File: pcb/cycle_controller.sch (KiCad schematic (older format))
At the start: 38 parts

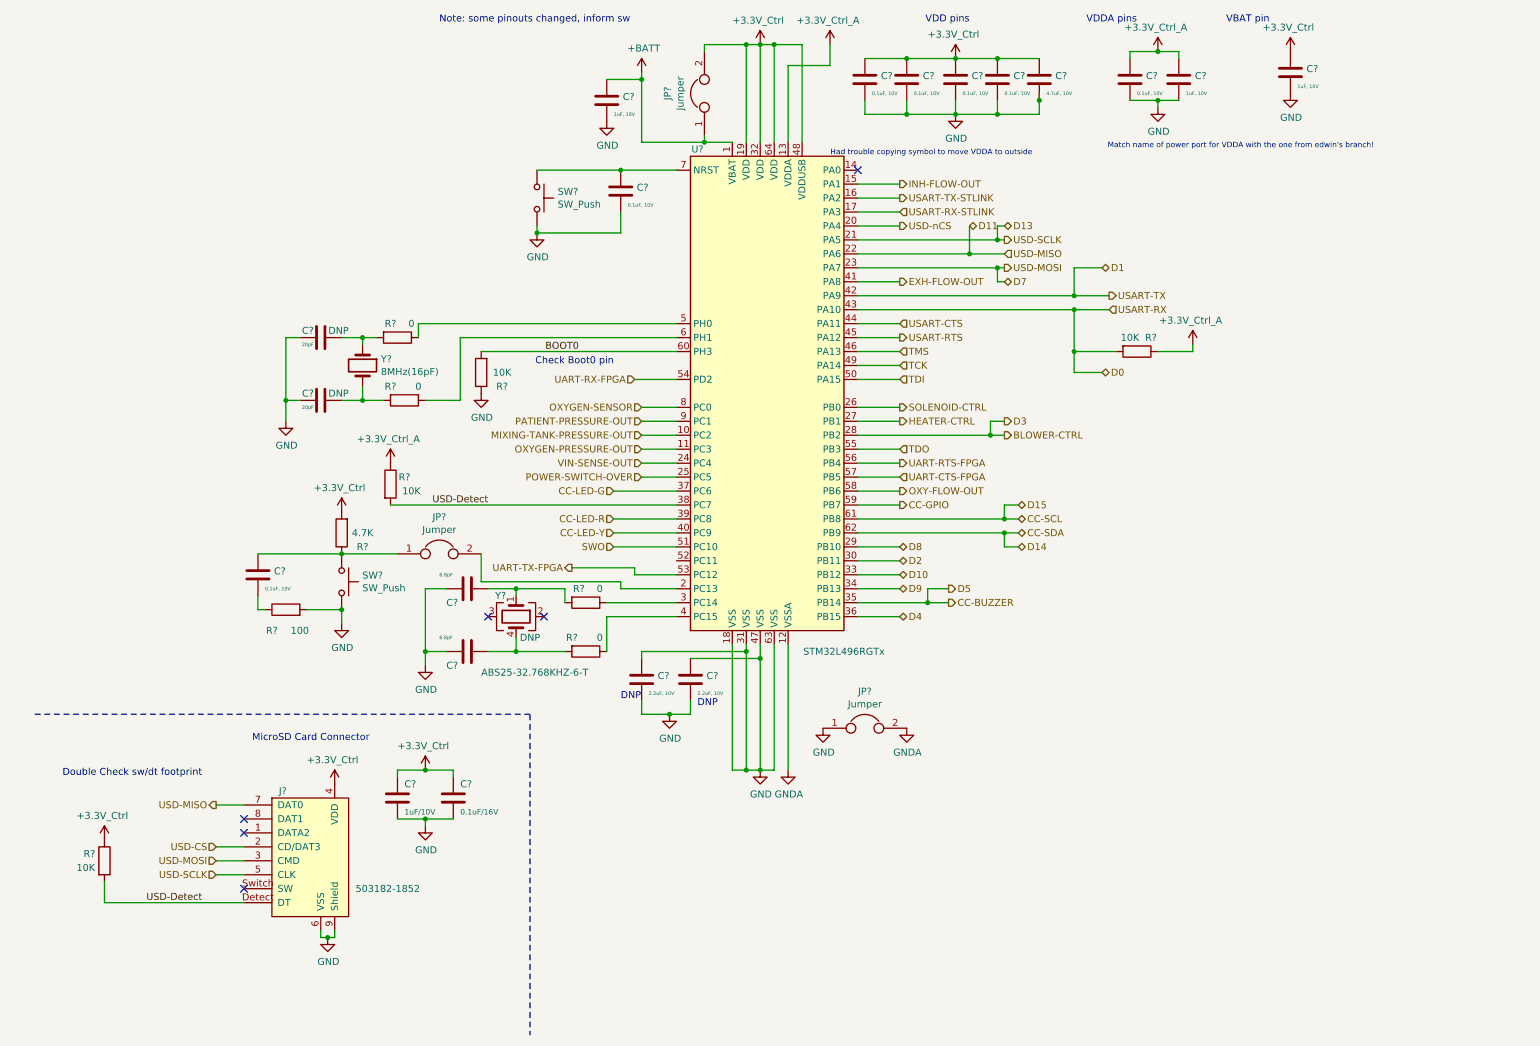
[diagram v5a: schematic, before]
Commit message: cycle controller updates, added headers to page
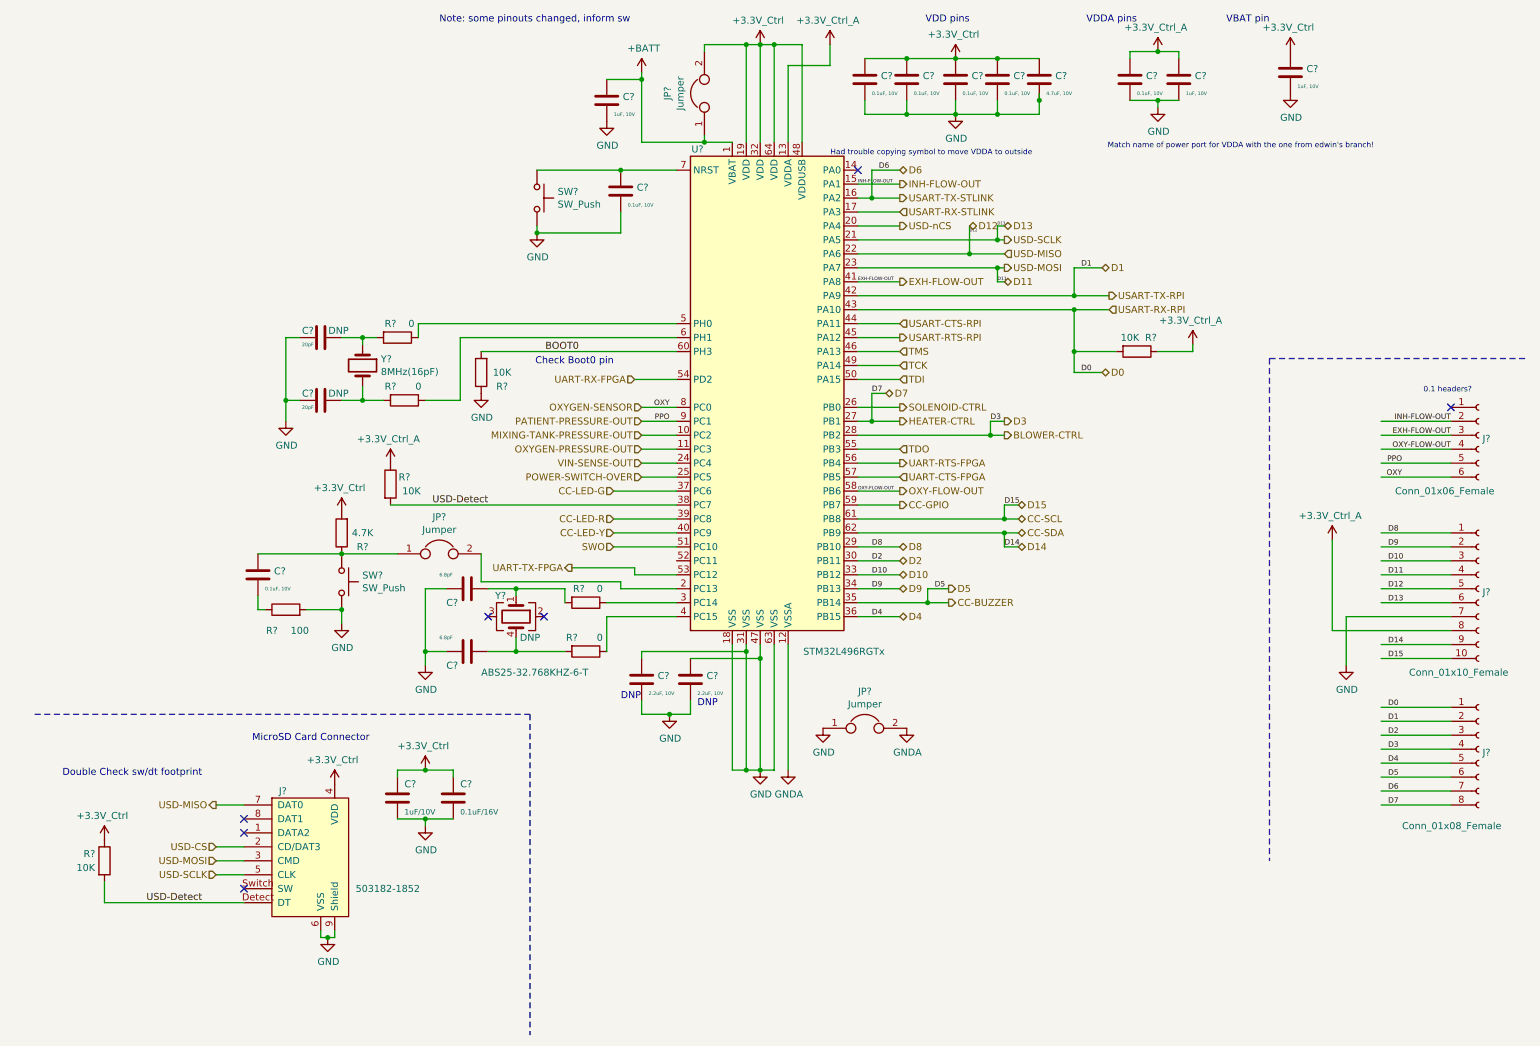
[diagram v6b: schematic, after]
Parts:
- added J?: Conn_01x10_Female, symbol Connector:Conn_01x10_Female
- added J?: Conn_01x08_Female, symbol Connector:Conn_01x08_Female
- added J?: Conn_01x06_Female, symbol Connector:Conn_01x06_Female
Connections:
- net labels added: D12, D6, OXY, PPO, USART-CTS-RPI, USART-RTS-RPI, USART-RX-RPI, USART-TX-RPI
- net labels removed: USART-CTS, USART-RTS, USART-RX, USART-TX
- wire segments 194 -> 225
- no-connect marks 6 -> 7
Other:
- note added: "0.1 headers?"
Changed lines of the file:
@@
 NoConn ~ 3750 4800
 Text HLabel 8200 2500 2    50   Output ~ 0
-USART-TX
+USART-TX-RPI
 Text HLabel 8200 2600 2    50   Input ~ 0
-USART-RX
+USART-RX-RPI
 Text HLabel 6700 2700 2    50   Input ~ 0
-USART-CTS
+USART-CTS-RPI
 Text HLabel 6700 2800 2    50   Output ~ 0
-USART-RTS
+USART-RTS-RPI
 Wire Wire Line
 	8200 2600 7950 2600
@@
 USART-RX-STLINK
 Wire Wire Line
-	6400 1800 6700 1800
+	6400 1800 6500 1800
 Wire Wire Line
 	6400 1900 6700 1900
@@
 	6400 3300 6700 3300
 Wire Wire Line
-	6400 3400 6700 3400
+	6400 3400 6500 3400
 Text HLabel 7450 3500 2    50   Output ~ 0
 BLOWER-CTRL
@@
 	7450 3400 7350 3400
 Text HLabel 7450 2400 2    50   BiDi ~ 0
-D7
+D11
 Wire Wire Line
 	7400 2300 7450 2300
@@
 	7400 2400 7450 2400
 Text HLabel 7200 2000 2    50   BiDi ~ 0
-D11
+D12
 Wire Wire Line
 	7200 2200 7450 2200
@@
 Wire Wire Line
 	7950 2900 7950 3050
+$Comp
+L Connector:Conn_01x10_Female J?
+U 1 1 602AB666
+P 10850 4600
+F 0 "J?" H 10877 4576 50  0000 L CNN
+F 1 "Conn_01x10_Female" H 10350 4000 50  0000 L CNN
+F 2 "" H 10850 4600 50  0001 C CNN
+F 3 "~" H 10850 4600 50  0001 C CNN
+	1    10850 4600
+	1    0    0    -1
+$EndComp
+$Comp
+L Connector:Conn_01x08_Female J?
+U 1 1 602AB6F0
+P 10850 5750
+F 0 "J?" H 10877 5726 50  0000 L CNN
+F 1 "Conn_01x08_Female" H 10300 5200 50  0000 L CNN
+F 2 "" H 10850 5750 50  0001 C CNN
+F 3 "~" H 10850 5750 50  0001 C CNN
+	1    10850 5750
+	1    0    0    -1
+$EndComp
+$Comp
+L Connector:Conn_01x06_Female J?
+U 1 1 602AB793
+P 10850 3500
+F 0 "J?" H 10877 3476 50  0000 L CNN
+F 1 "Conn_01x06_Female" H 10250 3100 50  0000 L CNN
+F 2 "" H 10850 3500 50  0001 C CNN
+F 3 "~" H 10850 3500 50  0001 C CNN
+	1    10850 3500
+	1    0    0    -1
+$EndComp
+Text Notes 10800 3200 2    39   ~ 0
+0.1 headers?
+Wire Notes Line
+	9350 2950 9350 6550
+NoConn ~ 10650 3300
+Wire Wire Line
+	10650 3400 10150 3400
+Wire Wire Line
+	10650 3500 10150 3500
+Wire Wire Line
+	10650 3600 10150 3600
+Wire Wire Line
+	10650 3700 10150 3700
+Wire Wire Line
+	10650 3800 10150 3800
+Text Label 10650 3400 2    39   ~ 0
+INH-FLOW-OUT
+Text Label 6400 1700 0    24   ~ 0
+INH-FLOW-OUT
+Text Label 6400 2400 0    24   ~ 0
+EXH-FLOW-OUT
+Text Label 10650 3500 2    39   ~ 0
+EXH-FLOW-OUT
+Text Label 6400 3900 0    24   ~ 0
+OXY-FLOW-OUT
+Text Label 10650 3600 2    39   ~ 0
+OXY-FLOW-OUT
+Text Label 5050 3400 2    39   ~ 0
+PPO
+Text Label 10300 3700 2    39   ~ 0
+PPO
+Text Label 5050 3300 2    39   ~ 0
+OXY
+Text Label 10300 3800 2    39   ~ 0
+OXY
+Text HLabel 6600 3200 2    50   BiDi ~ 0
+D7
+Wire Wire Line
+	6600 3200 6500 3200
+Wire Wire Line
+	6500 3200 6500 3400
+Connection ~ 6500 3400
+Wire Wire Line
+	6500 3400 6700 3400
+Wire Wire Line
+	10650 4200 10150 4200
+Wire Wire Line
+	10650 4300 10150 4300
+Wire Wire Line
+	10650 4400 10150 4400
+Wire Wire Line
+	10650 4500 10150 4500
+Wire Wire Line
+	10650 4600 10150 4600
+Wire Wire Line
+	10650 4700 10150 4700
+Wire Wire Line
+	10650 5000 10150 5000
+Wire Wire Line
+	10650 5100 10150 5100
+Text Label 10200 4200 0    39   ~ 0
+D8
+Text Label 10200 4300 0    39   ~ 0
+D9
+Text Label 10200 4400 0    39   ~ 0
+D10
+Text Label 10200 4500 0    39   ~ 0
+D11
+Text Label 10200 4600 0    39   ~ 0
+D12
+Text Label 10200 4700 0    39   ~ 0
+D13
+Text Label 10200 5000 0    39   ~ 0
+D14
+Text Label 10200 5100 0    39   ~ 0
+D15
+$Comp
+L RespiraWorks:+3.3V_Ctrl_A #PWR?
+U 1 1 60390EE2
+P 9800 4250
+F 0 "#PWR?" H 9800 4250 50  0001 C CNN
+F 1 "+3.3V_Ctrl_A" H 9785 4423 50  0000 C CNN
+F 2 "" H 9800 4250 50  0001 C CNN
+F 3 "" H 9800 4250 50  0001 C CNN
+	1    9800 4250
+	1    0    0    -1
+$EndComp
+$Comp
+L power:GND #PWR?
+U 1 1 60390FBB
+P 9900 5150
+F 0 "#PWR?" H 9900 4900 50  0001 C CNN
+F 1 "GND" H 9905 4977 50  0000 C CNN
+F 2 "" H 9900 5150 50  0001 C CNN
+F 3 "" H 9900 5150 50  0001 C CNN
+	1    9900 5150
+	1    0    0    -1
+$EndComp
+Wire Wire Line
+	10650 4800 9900 4800
+Wire Wire Line
+	9900 4800 9900 5150
+Wire Wire Line
+	10650 4900 9800 4900
+Wire Wire Line
+	9800 4900 9800 4250
+Wire Notes Line
+	9350 2950 11200 2950
+Text Label 6500 4300 0    39   ~ 0
+D8
+Text Label 6500 4600 0    39   ~ 0
+D9
+Text Label 6500 4500 0    39   ~ 0
+D10
+Text Label 6500 4400 0    39   ~ 0
+D2
+Text Label 6500 4800 0    39   ~ 0
+D4
+Text Label 7450 4300 0    39   ~ 0
+D14
+Text Label 7450 4000 0    39   ~ 0
+D15
+Text Label 7350 3400 0    39   ~ 0
+D3
+Text Label 6500 3200 0    39   ~ 0
+D7
+Text Label 8000 3050 0    39   ~ 0
+D0
+Text Label 8000 2300 0    39   ~ 0
+D1
+Text Label 7400 2400 0    24   ~ 0
+D11
+Text Label 7400 2000 0    20   ~ 0
+D13
+Text Label 7200 2050 0    20   ~ 0
+D12
+Wire Wire Line
+	10650 5450 10150 5450
+Wire Wire Line
+	10650 5550 10150 5550
+Wire Wire Line
+	10650 5650 10150 5650
+Wire Wire Line
+	10650 5750 10150 5750
+Wire Wire Line
+	10650 5850 10150 5850
+Wire Wire Line
+	10650 5950 10150 5950
+Wire Wire Line
+	10650 6050 10150 6050
+Wire Wire Line
+	10650 6150 10150 6150
+Text Label 10200 5450 0    39   ~ 0
+D0
+Text Label 10200 5550 0    39   ~ 0
+D1
+Text Label 10200 5650 0    39   ~ 0
+D2
+Text Label 10200 5750 0    39   ~ 0
+D3
+Text Label 10200 5850 0    39   ~ 0
+D4
+Text Label 10200 6150 0    39   ~ 0
+D7
+Text Label 6950 4600 0    39   ~ 0
+D5
+Text Label 10200 5950 0    39   ~ 0
+D5
+Text HLabel 6700 1600 2    50   BiDi ~ 0
+D6
+Wire Wire Line
+	6700 1600 6500 1600
+Wire Wire Line
+	6500 1600 6500 1800
+Connection ~ 6500 1800
+Wire Wire Line
+	6500 1800 6700 1800
+Text Label 6550 1600 0    39   ~ 0
+D6
+Text Label 10200 6050 0    39   ~ 0
+D6
 $EndSCHEMATC

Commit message: ui computer
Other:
- moved on the sheet: C?, J?, R?
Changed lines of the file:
@@
 L RespiraWorks:503182-1852 J?
 U 1 1 6016937E
-P 2450 6400
+P 2500 6650
 AR Path="/5FCD4D4C/6016937E" Ref="J?"  Part="1"
 AR Path="/5FCD4D18/6016937E" Ref="J?"  Part="1"
-F 0 "J?" H 2250 6750 50  0000 L CNN
-F 1 "503182-1852" H 2800 6050 50  0000 L CNN
-F 2 "RespiraWorks:5031821852" H 3250 6000 50  0001 C CNN
-F 3 "https://www.molex.com/pdm_docs/sd/5031821852_sd.pdf" H 3850 5900 50  0001 C CNN
-	1    2450 6400
+F 0 "J?" H 2300 7000 50  0000 L CNN
+F 1 "503182-1852" H 2850 6300 50  0000 L CNN
+F 2 "RespiraWorks:5031821852" H 3300 6250 50  0001 C CNN
+F 3 "https://www.molex.com/pdm_docs/sd/5031821852_sd.pdf" H 3900 6150 50  0001 C CNN
+	1    2500 6650
 	1    0    0    -1
 $EndComp
-Text Notes 2900 5700 2    50   ~ 0
+Text Notes 2950 5950 2    50   ~ 0
 MicroSD Card Connector
 $Comp
 L RespiraWorks:+3.3V_Ctrl #PWR?
 U 1 1 60169386
-P 2650 6000
+P 2700 6250
 AR Path="/5FCD4D4C/60169386" Ref="#PWR?"  Part="1"
 AR Path="/5FCD4D18/60169386" Ref="#PWR?"  Part="1"
-F 0 "#PWR?" H 2650 6000 50  0001 C CNN
-F 1 "+3.3V_Ctrl" H 2635 6173 50  0000 C CNN
-F 2 "" H 2650 6000 50  0001 C CNN
-F 3 "" H 2650 6000 50  0001 C CNN
-	1    2650 6000
+F 0 "#PWR?" H 2700 6250 50  0001 C CNN
+F 1 "+3.3V_Ctrl" H 2685 6423 50  0000 C CNN
+F 2 "" H 2700 6250 50  0001 C CNN
+F 3 "" H 2700 6250 50  0001 C CNN
+	1    2700 6250
 	1    0    0    -1
 $EndComp
@@
 L Device:C C?
 U 1 1 6016938C
-P 3100 6100
+P 3150 6350
 AR Path="/5FCD4D4C/6016938C" Ref="C?"  Part="1"
 AR Path="/5FCD4D18/6016938C" Ref="C?"  Part="1"
-F 0 "C?" H 3150 6200 50  0000 L CNN
-F 1 "1uF/10V" H 3150 6000 39  0000 L CNN
-F 2 "" H 3138 5950 50  0001 C CNN
-F 3 "~" H 3100 6100 50  0001 C CNN
-	1    3100 6100
+F 0 "C?" H 3200 6450 50  0000 L CNN
+F 1 "1uF/10V" H 3200 6250 39  0000 L CNN
+F 2 "" H 3188 6200 50  0001 C CNN
+F 3 "~" H 3150 6350 50  0001 C CNN
+	1    3150 6350
 	1    0    0    -1
 $EndComp
@@
 L Device:C C?
 U 1 1 60169393
-P 3500 6100
+P 3550 6350
 AR Path="/5FCD4D4C/60169393" Ref="C?"  Part="1"
 AR Path="/5FCD4D18/60169393" Ref="C?"  Part="1"
-F 0 "C?" H 3550 6200 50  0000 L CNN
-F 1 "0.1uF/16V" H 3550 6000 39  0000 L CNN
-F 2 "" H 3538 5950 50  0001 C CNN
-F 3 "~" H 3500 6100 50  0001 C CNN
-	1    3500 6100
+F 0 "C?" H 3600 6450 50  0000 L CNN
+F 1 "0.1uF/16V" H 3600 6250 39  0000 L CNN
+F 2 "" H 3588 6200 50  0001 C CNN
+F 3 "~" H 3550 6350 50  0001 C CNN
+	1    3550 6350
 	1    0    0    -1
 $EndComp
@@
 L RespiraWorks:+3.3V_Ctrl #PWR?
 U 1 1 6016939A
-P 3300 5900
+P 3350 6150
 AR Path="/5FCD4D4C/6016939A" Ref="#PWR?"  Part="1"
 AR Path="/5FCD4D18/6016939A" Ref="#PWR?"  Part="1"
-F 0 "#PWR?" H 3300 5900 50  0001 C CNN
-F 1 "+3.3V_Ctrl" H 3285 6073 50  0000 C CNN
-F 2 "" H 3300 5900 50  0001 C CNN
-F 3 "" H 3300 5900 50  0001 C CNN
-	1    3300 5900
+F 0 "#PWR?" H 3350 6150 50  0001 C CNN
+F 1 "+3.3V_Ctrl" H 3335 6323 50  0000 C CNN
+F 2 "" H 3350 6150 50  0001 C CNN
+F 3 "" H 3350 6150 50  0001 C CNN
+	1    3350 6150
 	1    0    0    -1
 $EndComp
 Wire Wire Line
-	3100 5950 3100 5900
+	3150 6200 3150 6150
 Wire Wire Line
-	3100 5900 3300 5900
+	3150 6150 3350 6150
 Wire Wire Line
-	3300 5900 3500 5900
+	3350 6150 3550 6150
 Wire Wire Line
-	3500 5900 3500 5950
-Connection ~ 3300 5900
+	3550 6150 3550 6200
+Connection ~ 3350 6150
 $Comp
 L power:GND #PWR?
 U 1 1 601693A5
-P 3300 6300
+P 3350 6550
 AR Path="/5FCD4D4C/601693A5" Ref="#PWR?"  Part="1"
 AR Path="/5FCD4D18/601693A5" Ref="#PWR?"  Part="1"
-F 0 "#PWR?" H 3300 6050 50  0001 C CNN
-F 1 "GND" H 3305 6127 50  0000 C CNN
-F 2 "" H 3300 6300 50  0001 C CNN
-F 3 "" H 3300 6300 50  0001 C CNN
-	1    3300 6300
+F 0 "#PWR?" H 3350 6300 50  0001 C CNN
+F 1 "GND" H 3355 6377 50  0000 C CNN
+F 2 "" H 3350 6550 50  0001 C CNN
+F 3 "" H 3350 6550 50  0001 C CNN
+	1    3350 6550
 	1    0    0    -1
 $EndComp
 Wire Wire Line
-	3100 6250 3300 6250
+	3150 6500 3350 6500
 Wire Wire Line
-	3300 6250 3300 6300
+	3350 6500 3350 6550
 Wire Wire Line
-	3500 6250 3300 6250
-Connection ~ 3300 6250
+	3550 6500 3350 6500
+Connection ~ 3350 6500
 $Comp
 L power:GND #PWR?
 U 1 1 601693AF
-P 2600 7100
+P 2650 7350
 AR Path="/5FCD4D4C/601693AF" Ref="#PWR?"  Part="1"
 AR Path="/5FCD4D18/601693AF" Ref="#PWR?"  Part="1"
-F 0 "#PWR?" H 2600 6850 50  0001 C CNN
-F 1 "GND" H 2605 6927 50  0000 C CNN
-F 2 "" H 2600 7100 50  0001 C CNN
-F 3 "" H 2600 7100 50  0001 C CNN
-	1    2600 7100
+F 0 "#PWR?" H 2650 7100 50  0001 C CNN
+F 1 "GND" H 2655 7177 50  0000 C CNN
+F 2 "" H 2650 7350 50  0001 C CNN
+F 3 "" H 2650 7350 50  0001 C CNN
+	1    2650 7350
 	1    0    0    -1
 $EndComp
 Wire Wire Line
-	2600 7100 2650 7100
+	2650 7350 2700 7350
 Wire Wire Line
-	2650 7100 2650 7050
+	2700 7350 2700 7300
 Wire Wire Line
-	2550 7050 2550 7100
+	2600 7300 2600 7350
 Wire Wire Line
-	2550 7100 2600 7100
-Connection ~ 2600 7100
-Text Notes 1700 5950 2    50   ~ 0
+	2600 7350 2650 7350
+Connection ~ 2650 7350
+Text Notes 1750 6200 2    50   ~ 0
 Double Check sw/dt footprint
-NoConn ~ 2000 6250
-NoConn ~ 2000 6350
-NoConn ~ 2000 6750
-Text Label 1700 6850 2    50   ~ 0
+NoConn ~ 2050 6500
+NoConn ~ 2050 6600
+NoConn ~ 2050 7000
+Text Label 1750 7100 2    50   ~ 0
 USD-Detect
 Wire Wire Line
-	1000 6850 2000 6850
+	1050 7100 2050 7100
 Wire Wire Line
-	1000 6850 1000 6700
+	1050 7100 1050 6950
 $Comp
 L Device:R R?
 U 1 1 601693C1
-P 1000 6550
+P 1050 6800
 AR Path="/5FCD4D4C/601693C1" Ref="R?"  Part="1"
 AR Path="/5FCD4D18/601693C1" Ref="R?"  Part="1"
-F 0 "R?" H 850 6600 50  0000 L CNN
-F 1 "10K" H 800 6500 50  0000 L CNN
-F 2 "RespiraWorks_std:R_0603_1608Metric" V 930 6550 50  0001 C CNN
-F 3 "~" H 1000 6550 50  0001 C CNN
-	1    1000 6550
+F 0 "R?" H 900 6850 50  0000 L CNN
+F 1 "10K" H 850 6750 50  0000 L CNN
+F 2 "RespiraWorks_std:R_0603_1608Metric" V 980 6800 50  0001 C CNN
+F 3 "~" H 1050 6800 50  0001 C CNN
+	1    1050 6800
 	1    0    0    -1
 $EndComp
@@
 L RespiraWorks:+3.3V_Ctrl #PWR?
 U 1 1 601693C8
-P 1000 6400
+P 1050 6650
 AR Path="/5FCD4D4C/601693C8" Ref="#PWR?"  Part="1"
 AR Path="/5FCD4D18/601693C8" Ref="#PWR?"  Part="1"
-F 0 "#PWR?" H 1000 6400 50  0001 C CNN
-F 1 "+3.3V_Ctrl" H 985 6573 50  0000 C CNN
-F 2 "" H 1000 6400 50  0001 C CNN
-F 3 "" H 1000 6400 50  0001 C CNN
-	1    1000 6400
+F 0 "#PWR?" H 1050 6650 50  0001 C CNN
+F 1 "+3.3V_Ctrl" H 1035 6823 50  0000 C CNN
+F 2 "" H 1050 6650 50  0001 C CNN
+F 3 "" H 1050 6650 50  0001 C CNN
+	1    1050 6650
 	1    0    0    -1
 $EndComp
 Wire Wire Line
-	2000 6650 1800 6650
+	2050 6900 1850 6900
 Wire Wire Line
-	2000 6550 1800 6550
+	2050 6800 1850 6800
 Wire Wire Line
-	2000 6450 1800 6450
+	2050 6700 1850 6700
 Wire Wire Line
-	2000 6150 1800 6150
-Text HLabel 1800 6150 0    50   Output ~ 0
+	2050 6400 1850 6400
+Text HLabel 1850 6400 0    50   Output ~ 0
 USD-MISO
-Text HLabel 1800 6450 0    50   Input ~ 0
+Text HLabel 1850 6700 0    50   Input ~ 0
 USD-CS
-Text HLabel 1800 6550 0    50   Input ~ 0
+Text HLabel 1850 6800 0    50   Input ~ 0
 USD-MOSI
-Text HLabel 1800 6650 0    50   Input ~ 0
+Text HLabel 1850 6900 0    50   Input ~ 0
 USD-SCLK
 Wire Notes Line
-	500  5500 4050 5500
+	500  5850 4050 5850
 Wire Notes Line
-	4050 5500 4050 7800
+	4050 5850 4050 7800
 NoConn ~ 6400 1600
 Wire Wire Line

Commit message: modified cycle controller and slightly ui
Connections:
- net labels removed: USD-nCS
- wire segments 225 -> 191
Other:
- moved on the sheet: R?
